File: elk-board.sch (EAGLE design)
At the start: 199 parts, among them IC1 ALLWINNER--H3, IC2 SY6280, IC3 K4B4G1646B-BCK0, IC4 RT8059GJ5, IC5 RT8059GJ5, IC6 SY8089A, IC7 NCP803SN263T1G, IC8 RT8059GJ5, IC9 MP2143DJ-LF-P, Q1 AO3415A, Q2 BCM856BS, Q3 9HT10-32.768KEZF-T, Q4 L2N7002WT1G, U1 AP6212, U2 STM32F411CEU6TR, X1 10118192-0001LF, X2 ST11-H, X3 IPEX-20279-001E, Y1 26MHz, Y2 24MHz

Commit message: Added emmc chip and integrated antenna
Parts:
- removed R53: 10K ohm, GHI-BasicComponents:RESISTOR-(INCH)-0402
- removed R54: 100K ohm, GHI-BasicComponents:RESISTOR-(INCH)-0402
- removed X2: ST11-H, JAE_By_element14_Batch_1:ST11-H
- removed X3: IPEX-20279-001E, Spark:IPEX-20279-001E
- added ANT1: AMCA31-2R450G-S1F-T3, AMCA31-2R450G-S1F-T3:AMCA31-2R450G-S1F-T3
- added C107, C108: 100nF, GHI-BasicComponents:CAPACITOR-(INCH)-0402
- added IC10: MP2143DJ-LF-P, MP2143DJ-LF-P:MP2143DJ-LF-P
- added L7: DFE252010P-2R2M=P2, DFE252010P-2R2M=P2:DFE252010P-2R2M=P2
- C1, C55, C7, C74, C79, C82: value 1uF -> 100nF
- C100, C25, C34, C44, C45, C56, C59, C66, C72, C73, C93, C96, C97: value 100nF -> 10uF; device GHI-BasicComponents:CAPACITOR-(INCH)-0402 -> GHI-BasicComponents:CAPACITOR-(INCH)-0603
- C101: value 22pF -> 10uF; device GHI-BasicComponents:CAPACITOR-(INCH)-0402 -> GHI-BasicComponents:CAPACITOR-(INCH)-0603
- C103: value 10uF -> 22pF; device GHI-BasicComponents:TOLBA_CAP -> GHI-BasicComponents:CAPACITOR-(INCH)-0402
- C104: value 10uF -> 100nF; device GHI-BasicComponents:TOLBA_CAP -> GHI-BasicComponents:CAPACITOR-(INCH)-0402
- C105, C106: value 100nF -> 10uF; device GHI-BasicComponents:CAPACITOR-(INCH)-0402 -> GHI-BasicComponents:TOLBA_CAP
- C12, C13, C47, C48: value 12pF -> 100nF
- C14: value 10uF -> 12pF; device GHI-BasicComponents:CAPACITOR-(INCH)-0603 -> GHI-BasicComponents:CAPACITOR-(INCH)-0402
- C15: value 10uF -> 12pF; device GHI-BasicComponents:TOLBA_CAP -> GHI-BasicComponents:CAPACITOR-(INCH)-0402
- C16: device GHI-BasicComponents:TOLBA_CAP -> GHI-BasicComponents:CAPACITOR-(INCH)-0603
- C17, C18: value 1uF -> 10uF; device GHI-BasicComponents:CAPACITOR-(INCH)-0402 -> GHI-BasicComponents:TOLBA_CAP
- C19: value 10pF -> 1uF
- C2, C23, C76, C8, C81, C84, C9: value 100nF -> 1uF
- C22: value 10uF -> 1.5pF; device GHI-BasicComponents:CAPACITOR-(INCH)-0603 -> GHI-BasicComponents:CAPACITOR-(INCH)-0402
- C24, C38, C4, C54, C61, C70, C92, C95, C98, C99: value 10uF -> 100nF; device GHI-BasicComponents:CAPACITOR-(INCH)-0603 -> GHI-BasicComponents:CAPACITOR-(INCH)-0402
- C27: value 100nF -> (none)
- C31: value 22uF -> 100nF; device GHI-BasicComponents:CAPACITOR-(INCH)-0603 -> GHI-BasicComponents:CAPACITOR-(INCH)-0402
- C32: value 10uF -> 22uF
- C37, C51, C58, C89: value 4.7uF -> 100nF
- C39, C91: value 10uF -> 4.7uF; device GHI-BasicComponents:CAPACITOR-(INCH)-0603 -> GHI-BasicComponents:CAPACITOR-(INCH)-0402
- C49, C50: value 100nF -> 12pF
- C5, C65: value 1uF -> 10uF; device GHI-BasicComponents:CAPACITOR-(INCH)-0402 -> GHI-BasicComponents:CAPACITOR-(INCH)-0603
- C53: value 100nF -> 4.7uF
- C57, C62, C69: value 10uF -> 1uF; device GHI-BasicComponents:CAPACITOR-(INCH)-0603 -> GHI-BasicComponents:CAPACITOR-(INCH)-0402
- C60: value 1uF -> 4.7uF
- C85, C86: value 18pF -> 100nF
- C87, C88: value 100nF -> 18pF
- IC1: value ALLWINNER--H3 -> KLM8G1GESD-B03P; device Allwinner_H3:ALLWINNER--H3 -> KLM8G1GESD-B03P:KLM8G1GESD-B03P
- IC2: value SY6280 -> ALLWINNER--H3; device SY6280:SY6280 -> Allwinner_H3:ALLWINNER--H3
- IC3: value K4B4G1646B-BCK0 -> SY6280; device K4B4G1646B-BCK0:K4B4G1646B-BCK0 -> SY6280:SY6280
- IC4: value RT8059GJ5 -> K4B4G1646B-BCK0; device RT8059GJ5:RT8059GJ5 -> K4B4G1646B-BCK0:K4B4G1646B-BCK0
- IC6: value SY8089A -> RT8059GJ5; device SY8089A:SY8089A -> RT8059GJ5:RT8059GJ5
- IC7: value NCP803SN263T1G -> SY8089A; device NCP803SN263T1G:NCP803SN263T1G -> SY8089A:SY8089A
- IC8: value RT8059GJ5 -> NCP803SN263T1G; device RT8059GJ5:RT8059GJ5 -> NCP803SN263T1G:NCP803SN263T1G
- IC9: value MP2143DJ-LF-P -> RT8059GJ5; device MP2143DJ-LF-P:MP2143DJ-LF-P -> RT8059GJ5:RT8059GJ5
- L2: value DFE252010P-2R2M=P2 -> 3.9nH; device DFE252010P-2R2M=P2:DFE252010P-2R2M=P2 -> Adafruit PowerBoost 1000C Rev B:MICROBUILDER_INDUCTOR_0402
- R10: value 22 ohm -> 100K ohm
- R14: value 33 ohm -> 6.8K ohm
- R15: value 6.8K ohm -> 10K ohm
- R16: value 10K ohm -> 2K ohm / 1%
- R18: value 2K ohm / 1% -> 100 ohm
- R19: value 100 ohm -> 10K ohm
- R24: value 10K ohm -> 10M ohm
- R25: value 10M ohm -> 6.8K ohm / 1%
- R26: value 6.8K ohm / 1% -> 47K ohm
- R27: value 47K ohm -> 240 ohm / 1%
- R29: value 240 ohm / 1% -> 10K ohm / 1%
- R3, R6: value 30K ohm -> 10K ohm
- R31, R36, R50: value 10K ohm / 1% -> 10K ohm
- R32: value 10K ohm -> 30K ohm / 1%
- R33: value 30K ohm / 1% -> 100K ohm
- R34: value 100K ohm -> 15K ohm / 1%
- R35: value 15K ohm / 1% -> 10K ohm / 1%
- R39: value 10K ohm -> 33 ohm
- R40: value 33 ohm -> 10K ohm
- R41: value 10K ohm -> 1K ohm
- R43: value 1K ohm -> 240 ohm / 1%
- R44: value 240 ohm / 1% -> 6.8K ohm / 1%
- R45: value 6.8K ohm / 1% -> 30K ohm / 1%
- R46: value 0 ohm -> 12K ohm / 1%
- R47: value 30K ohm / 1% -> 10K ohm / 1%
- R48: value 1K ohm -> 30K ohm / 1%
- R49: value 12K ohm / 1% -> 1K ohm
- R5: value 10K ohm -> 30K ohm
- R51: value 30K ohm / 1% -> 0 ohm
- R7: value 47K ohm -> 30K ohm
- R8: value 47K ohm -> 100K ohm
- R9: value 100K ohm -> 22 ohm
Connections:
- removed net N$15: C19.P$1, U1.WL_BT_ANT
- removed net N$16: C19.P$2, X3.1
- removed net N$30: R14.1, X2.CLK
- removed net SDC0_CLK: IC1G$1.PF2/SDC0_CLK/UART0_TX, R14.2
- removed net SDC0_CMD: IC1G$1.PF3/SDC0_CMD/JTAG_DO0, R8.1, X2.CMD
- removed net SDC0_D0: IC1G$1.PF1/SDC0_D0/JTAG_DI0, X2.DATA0
- removed net SDC0_D1: IC1G$1.PF0/SDC0_D1/JTAG_MS0, X2.DATA1
- removed net SDC0_D2: IC1G$1.PF5/SDC0_D2/JTAG_CK0, X2.DATA2
- removed net SDC0_D3: IC1G$1.PF4/SDC0_D3/UART0_RX, X2.CD/DATA3
- removed net SDC0_DET: IC1G$1.PF6, R7.1, X2.DSW2
- new net EMMC_CLK: IC1.CLK, IC2G$4.PC5/NAND_RE/SDC2_CLK
- new net EMMC_CMD: IC1.CMD, IC2G$4.PC6/NAND_RB0/SDC2_CMD, R3.1
- new net EMMC_D0: IC1.DAT0, IC2G$4.PC8/NAND_DQ0/SDC2_D0
- new net EMMC_D1: IC1.DAT1, IC2G$4.PC9/NAND_DQ1/SDC2_D1
- new net EMMC_D2: IC1.DAT2, IC2G$4.PC10/NAND_DQ2/SDC2_D2
- new net EMMC_D3: IC1.DAT3, IC2G$4.PC11/NAND_DQ3/SDC2_D3
- new net EMMC_D4: IC1.DAT4, IC2G$4.PC12/NAND_DQ4/SDC2_D4
- new net EMMC_D5: IC1.DAT5, IC2G$4.PC13/NAND_DQ5/SDC2_D5
- new net EMMC_D6: IC1.DAT6, IC2G$4.PC14/NAND_DQ6/SDC2_D6
- new net EMMC_D7: IC1.DAT7, IC2G$4.PC15/NAND_DQ7/SDC2_D7
- new net EMMC_RST: IC1.RSTN, IC2G$4.PC16/NAND_DQS/SDC2_RST
- new net N$12: ANT1.FEED, C27.P$2, L2.2
- new net N$20: C22.P$2, L2.1, U1.WL_BT_ANT
- new net VDDI_EMMC: C3.P$2, C7.P$2, IC1.VDDI
- net 1.2V: now also C19.P$1, C20.P$1, C23.P$1, C26.P$1, C29.P$1, C66.P$1, C72.P$1, C78.P$1, IC2G$2.EPHY_VDD, IC2G$6.VDD_SYS0, IC2G$6.VDD_SYS1, IC2G$6.VDD_SYS10, IC2G$6.VDD_SYS11, IC2G$6.VDD_SYS2, IC2G$6.VDD_SYS3, IC2G$6.VDD_SYS4, IC2G$6.VDD_SYS5, IC2G$6.VDD_SYS6, IC2G$6.VDD_SYS7, IC2G$6.VDD_SYS8, IC2G$6.VDD_SYS9, L5.2, R35.2; no longer C17.P$1, C18.P$1, C21.P$1, C25.P$1, C28.P$1, C64.P$1, C70.P$1, C76.P$1, IC1G$2.EPHY_VDD, IC1G$6.VDD_SYS0, IC1G$6.VDD_SYS1, IC1G$6.VDD_SYS10, IC1G$6.VDD_SYS11, IC1G$6.VDD_SYS2, IC1G$6.VDD_SYS3, IC1G$6.VDD_SYS4, IC1G$6.VDD_SYS5, IC1G$6.VDD_SYS6, IC1G$6.VDD_SYS7, IC1G$6.VDD_SYS8, IC1G$6.VDD_SYS9, L3.2, R36.2
- net 1.5V: now also C11.P$1, C12.P$1, C37.P$1, C52.P$1, C56.P$1, C57.P$1, C6.P$1, C62.P$1, C65.P$1, C68.P$1, C76.P$1, C77.P$1, C80.P$1, C84.P$1, C85.P$1, C92.P$1, IC2G$3.VCC_DRAM0, IC2G$3.VCC_DRAM1, IC2G$3.VCC_DRAM10, IC2G$3.VCC_DRAM2, IC2G$3.VCC_DRAM3, IC2G$3.VCC_DRAM4, IC2G$3.VCC_DRAM5, IC2G$3.VCC_DRAM6, IC2G$3.VCC_DRAM7, IC2G$3.VCC_DRAM8, IC2G$3.VCC_DRAM9, IC4.VDDQ_1, IC4.VDDQ_2, IC4.VDDQ_3, IC4.VDDQ_4, IC4.VDDQ_5, IC4.VDDQ_6, IC4.VDDQ_7, IC4.VDDQ_8, IC4.VDDQ_9, IC4.VDD_1, IC4.VDD_2, IC4.VDD_3, IC4.VDD_4, IC4.VDD_5, IC4.VDD_6, IC4.VDD_7, IC4.VDD_8, IC4.VDD_9, R16.2, R34.2; no longer C10.P$1, C35.P$1, C5.P$1, C50.P$1, C53.P$1, C54.P$1, C59.P$1, C60.P$1, C66.P$1, C67.P$1, C7.P$1, C74.P$1, C78.P$1, C79.P$1, C82.P$1, C88.P$1, IC1G$3.VCC_DRAM0, IC1G$3.VCC_DRAM1, IC1G$3.VCC_DRAM10, IC1G$3.VCC_DRAM2, IC1G$3.VCC_DRAM3, IC1G$3.VCC_DRAM4, IC1G$3.VCC_DRAM5, IC1G$3.VCC_DRAM6, IC1G$3.VCC_DRAM7, IC1G$3.VCC_DRAM8, IC1G$3.VCC_DRAM9, IC3.VDDQ_1, IC3.VDDQ_2, IC3.VDDQ_3, IC3.VDDQ_4, IC3.VDDQ_5, IC3.VDDQ_6, IC3.VDDQ_7, IC3.VDDQ_8, IC3.VDDQ_9, IC3.VDD_1, IC3.VDD_2, IC3.VDD_3, IC3.VDD_4, IC3.VDD_5, IC3.VDD_6, IC3.VDD_7, IC3.VDD_8, IC3.VDD_9, R17.2, R35.2
- net 3.3V: now also C1.P$2, C10.P$1, C101.P$1, C102.P$1, C108.P$1, C13.P$1, C30.P$1, C34.P$1, C35.P$1, C5.P$1, C54.P$1, C74.P$1, IC1.VDDF_1, IC1.VDDF_2, IC1.VDDF_3, IC1.VDDF_4, IC1.VDD_1, IC1.VDD_2, IC1.VDD_3, IC1.VDD_4, IC1.VDD_5, IC2G$1.VCC_PD, IC2G$2.AVCC, IC2G$2.EPHY_VCC, IC2G$2.HVCC, IC2G$2.V33_TV, IC2G$5.VCC_PG, IC2G$6.VCC_IO0, IC2G$6.VCC_IO1, IC2G$6.VCC_IO2, IC2G$6.VCC_IO3, IC2G$6.VCC_IO4, IC2G$6.VCC_IO5, IC2G$7.VCC_PLL, IC2G$7.VCC_RTC, IC2G$7.VCC_USB, IC2G$7.VDD_EFUSE, IC8.VCC, L6.2, R21.2, R26.1, R3.2, R31.1, R33.1, R36.1, R40.1, R45.2, R5.1, R50.2, R52.1, R6.2, R7.1, R8.1; no longer C106.P$1, C11.P$1, C2.P$2, C22.P$1, C26.P$1, C29.P$1, C32.P$1, C4.P$1, C52.P$1, C6.P$1, C72.P$1, C98.P$1, C99.P$1, IC1G$1.VCC_PD, IC1G$2.AVCC, IC1G$2.EPHY_VCC, IC1G$2.HVCC, IC1G$2.V33_TV, IC1G$5.VCC_PG, IC1G$6.VCC_IO0, IC1G$6.VCC_IO1, IC1G$6.VCC_IO2, IC1G$6.VCC_IO3, IC1G$6.VCC_IO4, IC1G$6.VCC_IO5, IC1G$7.VCC_PLL, IC1G$7.VCC_RTC, IC1G$7.VCC_USB, IC1G$7.VDD_EFUSE, IC7.VCC, L5.2, R24.2, R27.1, R3.1, R32.1, R34.1, R39.1, R41.1, R47.2, R5.2, R52.2, R53.1, R6.1, R7.2, R8.2, R9.1, X2.VDD
- net AP_RESET#: now also C89.P$1, IC2G$7.RESET, IC8.!RESET, R38.2; no longer C87.P$1, IC1G$7.RESET, IC7.!RESET, R39.2
- net BOOT0: now also IC2G$5.PG8/UART1_RTS/PG_EINT8, R20.1; no longer IC1G$5.PG8/UART1_RTS/PG_EINT8, R21.1
- net CPUX_VSET: now also IC2G$4.PC7/NAND_RB1, R50.1; no longer IC1G$4.PC5/NAND_RE/SDC2_CLK, R52.1
- net GND: now also C1.P$1, C101.P$2, C107.P$2, C108.P$2, C12.P$2, C13.P$2, C14.P$1, C15.P$1, C19.P$2, C2.P$2, C22.P$1, C27.P$1, C3.P$1, C34.P$2, C35.P$2, C36.P$1, C7.P$1, C85.P$2, C86.P$2, C87.P$1, C88.P$1, IC1.VSS_1, IC1.VSS_10, IC1.VSS_11, IC1.VSS_2, IC1.VSS_3, IC1.VSS_4, IC1.VSS_5, IC1.VSS_6, IC1.VSS_7, IC1.VSS_8, IC1.VSS_9, IC10.AGND, IC10.PGND, IC2G$2.AGND, IC2G$2.GND_TV, IC2G$2.HGND, IC2G$6.GND_CPUXFB, IC2G$8.GND0, IC2G$8.GND1, IC2G$8.GND10, IC2G$8.GND11, IC2G$8.GND12, IC2G$8.GND13, IC2G$8.GND14, IC2G$8.GND15, IC2G$8.GND16, IC2G$8.GND17, IC2G$8.GND18, IC2G$8.GND19, IC2G$8.GND2, IC2G$8.GND20, IC2G$8.GND21, IC2G$8.GND22, IC2G$8.GND23, IC2G$8.GND24, IC2G$8.GND25, IC2G$8.GND26, IC2G$8.GND27, IC2G$8.GND28, IC2G$8.GND29, IC2G$8.GND3, IC2G$8.GND30, IC2G$8.GND31, IC2G$8.GND32, IC2G$8.GND33, IC2G$8.GND34, IC2G$8.GND35, IC2G$8.GND36, IC2G$8.GND37, IC2G$8.GND38, IC2G$8.GND39, IC2G$8.GND4, IC2G$8.GND40, IC2G$8.GND41, IC2G$8.GND42, IC2G$8.GND43, IC2G$8.GND44, IC2G$8.GND45, IC2G$8.GND46, IC2G$8.GND47, IC2G$8.GND5, IC2G$8.GND6, IC2G$8.GND7, IC2G$8.GND8, IC2G$8.GND9, IC3.GND, IC4.VSSQ_1, IC4.VSSQ_2, IC4.VSSQ_3, IC4.VSSQ_4, IC4.VSSQ_5, IC4.VSSQ_6, IC4.VSSQ_7, IC4.VSSQ_8, IC4.VSSQ_9, IC4.VSS_1, IC4.VSS_10, IC4.VSS_11, IC4.VSS_12, IC4.VSS_2, IC4.VSS_3, IC4.VSS_4, IC4.VSS_5, IC4.VSS_6, IC4.VSS_7, IC4.VSS_8, IC4.VSS_9, IC9.GND, R10.1, R14.1, R17.1, R20.2, R25.1, R27.2, R29.1, R41.2, R43.1, R46.1; no longer C1.P$2, C103.P$2, C12.P$1, C13.P$1, C14.P$2, C15.P$2, C2.P$1, C22.P$2, C27.P$2, C3.P$2, C34.P$1, C36.P$2, C37.P$2, C7.P$2, C85.P$1, C86.P$1, C87.P$2, C88.P$2, IC1G$2.AGND, IC1G$2.GND_TV, IC1G$2.HGND, IC1G$6.GND_CPUXFB, IC1G$8.GND0, IC1G$8.GND1, IC1G$8.GND10, IC1G$8.GND11, IC1G$8.GND12, IC1G$8.GND13, IC1G$8.GND14, IC1G$8.GND15, IC1G$8.GND16, IC1G$8.GND17, IC1G$8.GND18, IC1G$8.GND19, IC1G$8.GND2, IC1G$8.GND20, IC1G$8.GND21, IC1G$8.GND22, IC1G$8.GND23, IC1G$8.GND24, IC1G$8.GND25, IC1G$8.GND26, IC1G$8.GND27, IC1G$8.GND28, IC1G$8.GND29, IC1G$8.GND3, IC1G$8.GND30, IC1G$8.GND31, IC1G$8.GND32, IC1G$8.GND33, IC1G$8.GND34, IC1G$8.GND35, IC1G$8.GND36, IC1G$8.GND37, IC1G$8.GND38, IC1G$8.GND39, IC1G$8.GND4, IC1G$8.GND40, IC1G$8.GND41, IC1G$8.GND42, IC1G$8.GND43, IC1G$8.GND44, IC1G$8.GND45, IC1G$8.GND46, IC1G$8.GND47, IC1G$8.GND5, IC1G$8.GND6, IC1G$8.GND7, IC1G$8.GND8, IC1G$8.GND9, IC2.GND, IC3.VSSQ_1, IC3.VSSQ_2, IC3.VSSQ_3, IC3.VSSQ_4, IC3.VSSQ_5, IC3.VSSQ_6, IC3.VSSQ_7, IC3.VSSQ_8, IC3.VSSQ_9, IC3.VSS_1, IC3.VSS_10, IC3.VSS_11, IC3.VSS_12, IC3.VSS_2, IC3.VSS_3, IC3.VSS_4, IC3.VSS_5, IC3.VSS_6, IC3.VSS_7, IC3.VSS_8, IC3.VSS_9, IC4.GND, IC9.AGND, IC9.PGND, R16.1, R18.1, R21.2, R26.1, R29.2, R31.1, R43.2, R45.1, R49.1, R54.1, X2.GND, X2.VSS, X3.GND@1
- net GPIOA15/SPI1_MOSI: now also IC2G$1.PA15/SPI1_MOSI/UART3_RTS/PA_EINT15, R39.1; no longer IC1G$1.PA15/SPI1_MOSI/UART3_RTS/PA_EINT15, R40.1
- net H3_UART1_RX: now also IC2G$5.PG7/UART1_RX/PG_EINT7; no longer IC1G$5.PG7/UART1_RX/PG_EINT7
- net H3_UART1_TX: now also IC2G$5.PG6/UART1_TX/PG_EINT6; no longer IC1G$5.PG6/UART1_TX/PG_EINT6
- net KERNEL_LED: now also IC2G$1.PD6/RGMII_NULL/MII_RXERR/RMII_RXER; no longer IC1G$1.PD6/RGMII_NULL/MII_RXERR/RMII_RXER
- net MCU_3.3V: now also C58.P$1, C59.P$1, C64.P$1, C67.P$1, C70.P$1, C79.P$1, C82.P$1, C86.P$1, C91.P$1, L3.2, R19.1, R32.2; no longer C56.P$1, C57.P$1, C62.P$1, C65.P$1, C68.P$1, C77.P$1, C80.P$1, C84.P$1, C89.P$1, L2.2, R20.1, R33.2
- net MCU_REG_EN: now also IC2G$1.PD1/RGMII_RXD2/MII_RXD2/RMII_NULL/DI_RX, IC5.EN, R21.1; no longer IC1G$1.PD1/RGMII_RXD2/MII_RXD2/RMII_NULL/DI_RX, IC4.EN, R22.1
- net MCU_RST: now also C36.P$2, IC2G$5.PG13/PCM1_DIN/PG_EINT13, R19.2; no longer C34.P$2, IC1G$5.PG13/PCM1_DIN/PG_EINT13, R20.2
- net N$1: now also R9.1; no longer R10.1
- net N$10: now also C14.P$2; no longer C12.P$2
- net N$11: now also R49.2; no longer R48.2
- net N$13: now also R39.2; no longer R40.2
- net N$14: now also C25.P$1; no longer C24.P$1
- net N$18: now also IC6.FB, R29.2, R34.1; no longer IC5.FB, R30.2, R35.1
- net N$19: now also IC7.LX, L5.1; no longer IC6.LX, L3.1
- net N$2: now also R51.2; no longer R46.2
- net N$21: now also R41.1; no longer R42.1
- net N$22: now also C39.P$1; no longer C37.P$1
- net N$26: now also IC4.ZQ, R27.1; no longer IC3.ZQ, R28.1
- net N$28: now also C16.P$1, IC3.OUT; no longer C14.P$1, IC2.OUT
- net N$3: now also IC5.LX, L3.1; no longer IC4.LX, L2.1
- net N$33: now also IC7.FB, R30.2, R35.1; no longer IC6.FB, R31.2, R36.1
- net N$35: now also C49.P$1, IC2G$7.X32KIN, R24.2; no longer C47.P$1, IC1G$7.X32KIN, R25.2
- net N$36: now also IC10.SW, L7.1; no longer IC9.SW, L6.1
- net N$37: now also C103.P$2, IC10.FB, R46.2, R47.1, R48.2; no longer C101.P$2, IC9.FB, R49.2, R50.1, R51.2
- net N$38: now also IC3.ISET, R14.2; no longer IC2.ISET, R15.2
- net N$40: now also IC9.LX, L6.1; no longer IC8.LX, L5.1
- net N$41: now also IC2G$3.SZQ, R43.2; no longer IC1G$3.SZQ, R44.2
- net N$42: now also IC9.FB, R44.2, R45.1; no longer IC8.FB, R45.2, R47.1
- net N$44: now also R48.1; no longer R51.1
- net N$48: now also C50.P$1, IC2G$7.X32KOUT, R24.1; no longer C48.P$1, IC1G$7.X32KOUT, R25.1
- net N$5: now also R42.1; no longer R43.1
- net N$50: now also C60.P$1, IC2G$7.VDD_EFUSEBP; no longer C58.P$1, IC1G$7.VDD_EFUSEBP
- net N$51: now also IC2G$7.NMI, R26.2; no longer IC1G$7.NMI, R27.2
- net N$52: now also IC2G$7.KEYADC, R33.2; no longer IC1G$7.KEYADC, R34.2
- net N$6: now also IC6.LX; no longer IC5.LX
- net N$7: now also R10.2; no longer R54.2
- net N$74: now also IC4.NC_4, R28.1; no longer IC3.NC_4, R29.1
- net N$8: now also IC5.FB, R25.2, R32.1; no longer IC4.FB, R26.2, R33.1
- net N$9: now also C15.P$2; no longer C13.P$2
- net PWR_DRAM: now also IC2G$1.PA21/PCM0_DIN/SIM_VPPPP/PA_EINT21, IC6.EN, R22.1; no longer IC1G$1.PA21/PCM0_DIN/SIM_VPPPP/PA_EINT21, IC5.EN, R23.1
- net PWR_STB: now also IC10.EN, IC2G$1.PD4/RGMII_RXCK/MII_RXCK/RMII_NULL, IC7.EN, R23.1; no longer IC1G$1.PD4/RGMII_RXCK/MII_RXCK/RMII_NULL, IC6.EN, IC9.EN, R24.1
- net RESET_SW: now also IC2G$1.PA8/SIM_DATA/PA_EINT8, R52.2; no longer IC1G$1.PA8/SIM_DATA/PA_EINT8, R53.2
- net SA0: now also IC2G$3.SA0, IC4.A0; no longer IC1G$3.SA0, IC3.A0
- net SA1: now also IC2G$3.SA1, IC4.A1; no longer IC1G$3.SA1, IC3.A1
- net SA10: now also IC2G$3.SA10, IC4.A10/AP; no longer IC1G$3.SA10, IC3.A10/AP
- net SA11: now also IC2G$3.SA11, IC4.A11; no longer IC1G$3.SA11, IC3.A11
- net SA12: now also IC2G$3.SA12, IC4.A12/!BC; no longer IC1G$3.SA12, IC3.A12/!BC
- net SA13: now also IC2G$3.SA13, IC4.A13; no longer IC1G$3.SA13, IC3.A13
- net SA14: now also IC2G$3.SA14, IC4.A14; no longer IC1G$3.SA14, IC3.A14
- net SA15: now also IC2G$3.SA15, IC4.NC_5; no longer IC1G$3.SA15, IC3.NC_5
- net SA2: now also IC2G$3.SA2, IC4.A2; no longer IC1G$3.SA2, IC3.A2
- net SA3: now also IC2G$3.SA3, IC4.A3; no longer IC1G$3.SA3, IC3.A3
- net SA4: now also IC2G$3.SA4, IC4.A4; no longer IC1G$3.SA4, IC3.A4
- net SA5: now also IC2G$3.SA5, IC4.A5; no longer IC1G$3.SA5, IC3.A5
- net SA6: now also IC2G$3.SA6, IC4.A6; no longer IC1G$3.SA6, IC3.A6
- net SA7: now also IC2G$3.SA7, IC4.A7; no longer IC1G$3.SA7, IC3.A7
- net SA8: now also IC2G$3.SA8, IC4.A8; no longer IC1G$3.SA8, IC3.A8
- net SA9: now also IC2G$3.SA9, IC4.A9; no longer IC1G$3.SA9, IC3.A9
- net SBA0: now also IC2G$3.SBA0, IC4.BA0; no longer IC1G$3.SBA0, IC3.BA0
- net SBA1: now also IC2G$3.SBA1, IC4.BA1; no longer IC1G$3.SBA1, IC3.BA1
- net SBA2: now also IC2G$3.SBA2, IC4.BA2; no longer IC1G$3.SBA2, IC3.BA2
- net SCAS: now also IC2G$3.SCAS, IC4.!CAS; no longer IC1G$3.SCAS, IC3.!CAS
- net SCKE0: now also IC2G$3.SCKE0, IC4.CKE; no longer IC1G$3.SCKE0, IC3.CKE
- net SCKE1: now also IC2G$3.SCKE1, IC4.NC_2; no longer IC1G$3.SCKE1, IC3.NC_2
- net SCK_N: now also IC2G$3.SCKB, IC4.!CK, R18.1; no longer IC1G$3.SCKB, IC3.!CK, R19.1
- net SCK_P: now also IC2G$3.SCK, IC4.CK, R18.2; no longer IC1G$3.SCK, IC3.CK, R19.2
- net SCS0: now also IC2G$3.SCS0, IC4.!CS; no longer IC1G$3.SCS0, IC3.!CS
- net SCS1: now also IC2G$3.SCS1, IC4.NC_3; no longer IC1G$3.SCS1, IC3.NC_3
- net SDC1_CLK: now also IC2G$5.PG0/SDC1_CLK/PG_EINT0, R9.2; no longer IC1G$5.PG0/SDC1_CLK/PG_EINT0, R10.2
- net SDC1_CMD: now also IC2G$5.PG1/SDC1_CMD/PG_EINT1, R7.2; no longer IC1G$5.PG1/SDC1_CMD/PG_EINT1, R6.2
- net SDC1_D0: now also IC2G$5.PG2/SDC1_D0/PG_EINT2, R5.2; no longer IC1G$5.PG2/SDC1_D0/PG_EINT2, R4.2
- net SDC1_D1: now also IC2G$5.PG3/SDC1_D1/PG_EINT3, R4.2; no longer IC1G$5.PG3/SDC1_D1/PG_EINT3, R3.2
- net SDC1_D2: now also IC2G$5.PG4/SDC1_D2/PG_EINT4; no longer IC1G$5.PG4/SDC1_D2/PG_EINT4
- net SDC1_D3: now also IC2G$5.PG5/SDC1_D3/PG_EINT5; no longer IC1G$5.PG5/SDC1_D3/PG_EINT5
- net SDQ0: now also IC2G$3.SDQ0, IC4.DQL1; no longer IC1G$3.SDQ0, IC3.DQL1
- net SDQ1: now also IC2G$3.SDQ1, IC4.DQL5; no longer IC1G$3.SDQ1, IC3.DQL5
- net SDQ10: now also IC2G$3.SDQ10, IC4.DQU7; no longer IC1G$3.SDQ10, IC3.DQU7
- net SDQ11: now also IC2G$3.SDQ11, IC4.DQU6; no longer IC1G$3.SDQ11, IC3.DQU6
- net SDQ12: now also IC2G$3.SDQ12, IC4.DQU2; no longer IC1G$3.SDQ12, IC3.DQU2
- net SDQ13: now also IC2G$3.SDQ13, IC4.DQU0; no longer IC1G$3.SDQ13, IC3.DQU0
- net SDQ14: now also IC2G$3.SDQ14, IC4.DQU1; no longer IC1G$3.SDQ14, IC3.DQU1
- net SDQ15: now also IC2G$3.SDQ15, IC4.DQU3; no longer IC1G$3.SDQ15, IC3.DQU3
- net SDQ2: now also IC2G$3.SDQ2, IC4.DQL3; no longer IC1G$3.SDQ2, IC3.DQL3
- net SDQ3: now also IC2G$3.SDQ3, IC4.DQL4; no longer IC1G$3.SDQ3, IC3.DQL4
- net SDQ4: now also IC2G$3.SDQ4, IC4.DQL7; no longer IC1G$3.SDQ4, IC3.DQL7
- net SDQ5: now also IC2G$3.SDQ5, IC4.DQL0; no longer IC1G$3.SDQ5, IC3.DQL0
- net SDQ6: now also IC2G$3.SDQ6, IC4.DQL6; no longer IC1G$3.SDQ6, IC3.DQL6
- net SDQ7: now also IC2G$3.SDQ7, IC4.DQL2; no longer IC1G$3.SDQ7, IC3.DQL2
- net SDQ8: now also IC2G$3.SDQ8, IC4.DQU4; no longer IC1G$3.SDQ8, IC3.DQU4
- net SDQ9: now also IC2G$3.SDQ9, IC4.DQU5; no longer IC1G$3.SDQ9, IC3.DQU5
- net SDQM0: now also IC2G$3.SDQM0, IC4.DML; no longer IC1G$3.SDQM0, IC3.DML
- net SDQM1: now also IC2G$3.SDQM1, IC4.DMU; no longer IC1G$3.SDQM1, IC3.DMU
- net SDQS0_N: now also IC2G$3.SDQSB0, IC4.!DQSL; no longer IC1G$3.SDQSB0, IC3.!DQSL
- net SDQS0_P: now also IC2G$3.SDQS0, IC4.DQSL; no longer IC1G$3.SDQS0, IC3.DQSL
- net SDQS1_N: now also IC2G$3.SDQSB1, IC4.!DQSU; no longer IC1G$3.SDQSB1, IC3.!DQSU
- net SDQS1_P: now also IC2G$3.SDQS1, IC4.DQSU; no longer IC1G$3.SDQS1, IC3.DQSU
- net SETUP_SW: now also IC2G$1.PA20/PCM0_DOUT/SIM_VPPEN/PA_EINT20, R40.2; no longer IC1G$1.PA20/PCM0_DOUT/SIM_VPPEN/PA_EINT20, R41.2
- net SODT0: now also IC2G$3.SODT0, IC4.ODT; no longer IC1G$3.SODT0, IC3.ODT
- net SODT1: now also IC2G$3.SODT1, IC4.NC_1; no longer IC1G$3.SODT1, IC3.NC_1
- net SRAS: now also IC2G$3.SRAS, IC4.!RAS; no longer IC1G$3.SRAS, IC3.!RAS
- net SRST: now also IC2G$3.SRST, IC4.!RESET; no longer IC1G$3.SRST, IC3.!RESET
- net SVREF: now also C104.P$1, C37.P$2, C38.P$1, C51.P$1, IC2G$3.SVREF, IC4.VREFCA, IC4.VREFDQ, R16.1, R17.2; no longer C102.P$1, C35.P$2, C36.P$1, C49.P$1, IC1G$3.SVREF, IC3.VREFCA, IC3.VREFDQ, R17.1, R18.2
- net SWE: now also IC2G$3.SWE, IC4.!WE; no longer IC1G$3.SWE, IC3.!WE
- net UART0_RX: now also IC2G$1.PA5/UART0_RX/PWM0/PA_EINT5, R51.1; no longer IC1G$1.PA5/UART0_RX/PWM0/PA_EINT5, R46.1
- net UART0_TX: now also IC2G$1.PA4/UART0_TX/PA_EINT4, R49.1; no longer IC1G$1.PA4/UART0_TX/PA_EINT4, R48.1
- net UBOOT: now also IC2G$7.UBOOT, R36.2; no longer IC1G$7.UBOOT, R38.2
- net USB0_DRVVBUS: now also IC2G$4.PC2/NAND_CLE/SPI0_CLK, IC3.EN, R15.2; no longer IC1G$4.PC11/NAND_DQ3/SDC2_D3, IC2.EN, R16.2
- net USB0_N: now also IC2G$7.USB_DM0; no longer IC1G$7.USB_DM0
- net USB0_OTGID: now also IC2G$5.PG12/PCM1_DOUT/PG_EINT12, R6.1; no longer IC1G$5.PG12/PCM1_DOUT/PG_EINT12, R5.1
- net USB0_P: now also IC2G$7.USB_DP0; no longer IC1G$7.USB_DP0
- net VDD_CPUFB: now also C103.P$1, IC2G$6.VDD_CPUXFB, R47.2; no longer C101.P$1, IC1G$6.VDD_CPUXFB, R50.2
- net VDD_CPUS: now also C2.P$1, C4.P$1, C53.P$1, IC2G$6.VDD_CPUS0, IC2G$6.VDD_CPUS1, IC2G$7.RTC_VIO; no longer C1.P$1, C3.P$1, C51.P$1, IC1G$6.VDD_CPUS0, IC1G$6.VDD_CPUS1, IC1G$7.RTC_VIO
- net VDD_CPUX: now also C106.P$1, C107.P$1, C17.P$1, C18.P$1, C21.P$1, C24.P$1, C28.P$1, C31.P$1, IC10.OUT, IC2G$6.VDD_CPUX0, IC2G$6.VDD_CPUX1, IC2G$6.VDD_CPUX10, IC2G$6.VDD_CPUX11, IC2G$6.VDD_CPUX12, IC2G$6.VDD_CPUX2, IC2G$6.VDD_CPUX3, IC2G$6.VDD_CPUX4, IC2G$6.VDD_CPUX5, IC2G$6.VDD_CPUX6, IC2G$6.VDD_CPUX7, IC2G$6.VDD_CPUX8, IC2G$6.VDD_CPUX9, L7.2; no longer C103.P$1, C104.P$1, C15.P$1, C16.P$1, C20.P$1, C23.P$1, C27.P$1, C30.P$1, IC1G$6.VDD_CPUX0, IC1G$6.VDD_CPUX1, IC1G$6.VDD_CPUX10, IC1G$6.VDD_CPUX11, IC1G$6.VDD_CPUX12, IC1G$6.VDD_CPUX2, IC1G$6.VDD_CPUX3, IC1G$6.VDD_CPUX4, IC1G$6.VDD_CPUX5, IC1G$6.VDD_CPUX6, IC1G$6.VDD_CPUX7, IC1G$6.VDD_CPUX8, IC1G$6.VDD_CPUX9, IC9.OUT, L6.2
- net VIN: now also C32.P$1, C47.P$1, C48.P$1, C98.P$1, C99.P$1, IC10.VIN, IC3.IN, IC6.VIN, IC7.IN, IC9.EN; no longer C31.P$1, C38.P$1, C39.P$1, C91.P$1, C92.P$1, IC2.IN, IC4.VIN, IC6.IN, IC8.EN, IC8.VIN
- net WIFI_32K: now also IC2G$7.X32KFOUT, R31.2; no longer IC1G$7.X32KFOUT, R32.2
- net WL_REG_ON: now also IC2G$9.PL7/S_JTAG_SI/S_PL_EINT7; no longer IC1G$9.PL7/S_JTAG_SI/S_PL_EINT7
- net WL_WAKE_HOST: now also IC2G$5.PG10/PCM1_SYNC/PG_EINT10, R8.2; no longer IC1G$5.PG10/PCM1_SYNC/PG_EINT10, R9.2
- net X24_IN: now also C87.P$2, IC2G$7.X24MIN; no longer C85.P$2, IC1G$7.X24MIN
- net X24_OUT: now also C88.P$2, IC2G$7.X24MOUT; no longer C86.P$2, IC1G$7.X24MOUT
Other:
- note removed: "Only DATA[0:3] need length matching"
- note removed: "uSD Connector"
- moved on the sheet: C1, C10, C100, C101, C102, C103, C104, C105, C106, C11, C12, C13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

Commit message: Finished emmc and antenna (WIP)
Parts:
- L2: device Adafruit PowerBoost 1000C Rev B:MICROBUILDER_INDUCTOR_0402 -> Nordic_nRF:INDUCTOR_0402_L
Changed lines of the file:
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@@
 </layers>
 <schematic xreflabel="%F%N/%S.%C%R" xrefpart="/%S.%C%R">
-<fusionteam huburn="a.YnVzaW5lc3M6ZWxrcmVt" projecturn="a.YnVzaW5lc3M6ZWxrcmVtIzIwMTkwNTE0MTkzNzY0NjI2" folderUrn="urn:adsk.wipprod:fs.folder:co.lM7F2dEtQpysUSzvypi4-Q" urn="urn:adsk.wipprod:dm.lineage:Se4qbmlATyubusVm2n9KuA"  versionUrn="urn:adsk.wipprod:fs.file:vf.Se4qbmlATyubusVm2n9KuA?version=24" camFileUrn="" camFileVersionUrn="" lastpublishedchangeguid="8b6fd80a-dbfd-1cff-e868-49cbea7d7d36"/>
+<fusionteam huburn="a.YnVzaW5lc3M6ZWxrcmVt" projecturn="a.YnVzaW5lc3M6ZWxrcmVtIzIwMTkwNTE0MTkzNzY0NjI2" folderUrn="urn:adsk.wipprod:fs.folder:co.U9XNDY5QRfqUZXJ892w5Yg" urn="urn:adsk.wipprod:dm.lineage:FdQPUJtxQbmN-6sV6-on_w"  versionUrn="urn:adsk.wipprod:fs.file:vf.FdQPUJtxQbmN-6sV6-on_w?version=2" camFileUrn="" camFileVersionUrn="" lastpublishedchangeguid="486159d2-3dfa-844d-1c70-05aee61310eb"/>
 <attributes>
 </attributes>
@@
 <part name="GND4" library="supply1" library_urn="urn:adsk.eagle:library:371" deviceset="GND" device=""/>
 <part name="3.3V4" library="microbuilder" deviceset="3.3V" device=""/>
-<part name="L2" library="Adafruit PowerBoost 1000C Rev B" deviceset="MICROBUILDER_INDUCTOR" device="_0402" value="3.9nH"/>
+<part name="L2" library="Nordic_nRF" deviceset="INDUCTOR" device="_0402_L" package3d_urn="urn:adsk.eagle:package:2593728/1" value="3.9nH"/>
 <part name="GND21" library="supply1" library_urn="urn:adsk.eagle:library:371" deviceset="GND" device=""/>
 <part name="ANT1" library="AMCA31-2R450G-S1F-T3" deviceset="AMCA31-2R450G-S1F-T3" device=""/>
@@
 <attribute name="VALUE" x="51.816" y="282.956" size="1.27" layer="96"/>
 </instance>
-<instance part="L2" gate="G$1" x="190.5" y="142.24" smashed="yes">
-<attribute name="NAME" x="190.5" y="144.78" size="1.27" layer="95" align="center"/>
-<attribute name="VALUE" x="190.5" y="140.7" size="1.27" layer="96" align="center"/>
+<instance part="L2" gate="L$1" x="190.5" y="142.24" smashed="yes" rot="R90">
+<attribute name="NAME" x="185.42" y="144.78" size="1.27" layer="95" rot="R180" align="center"/>
+<attribute name="VALUE" x="195.58" y="144.78" size="1.27" layer="96" rot="R180" align="center"/>
 </instance>
 <instance part="GND21" gate="1" x="177.8" y="129.54" smashed="yes">
@@
 <segment>
 <pinref part="U1" gate="G$1" pin="WL_BT_ANT"/>
-<pinref part="L2" gate="G$1" pin="1"/>
-<wire x1="185.42" y1="142.24" x2="177.8" y2="142.24" width="0.1524" layer="91"/>
+<pinref part="L2" gate="L$1" pin="1"/>
+<wire x1="182.88" y1="142.24" x2="177.8" y2="142.24" width="0.1524" layer="91"/>
 <wire x1="177.8" y1="142.24" x2="168.402" y2="142.24" width="0.1524" layer="91"/>
 <wire x1="168.402" y1="142.24" x2="168.402" y2="137.16" width="0.1524" layer="91"/>
@@
 <net name="N$12" class="0">
 <segment>
-<pinref part="L2" gate="G$1" pin="2"/>
+<pinref part="L2" gate="L$1" pin="2"/>
 <pinref part="ANT1" gate="G$1" pin="FEED"/>
-<wire x1="195.58" y1="142.24" x2="200.66" y2="142.24" width="0.1524" layer="91"/>
+<wire x1="198.12" y1="142.24" x2="200.66" y2="142.24" width="0.1524" layer="91"/>
 <pinref part="C27" gate="G$1" pin="P$2"/>
 <wire x1="200.66" y1="142.24" x2="208.28" y2="142.24" width="0.1524" layer="91"/>

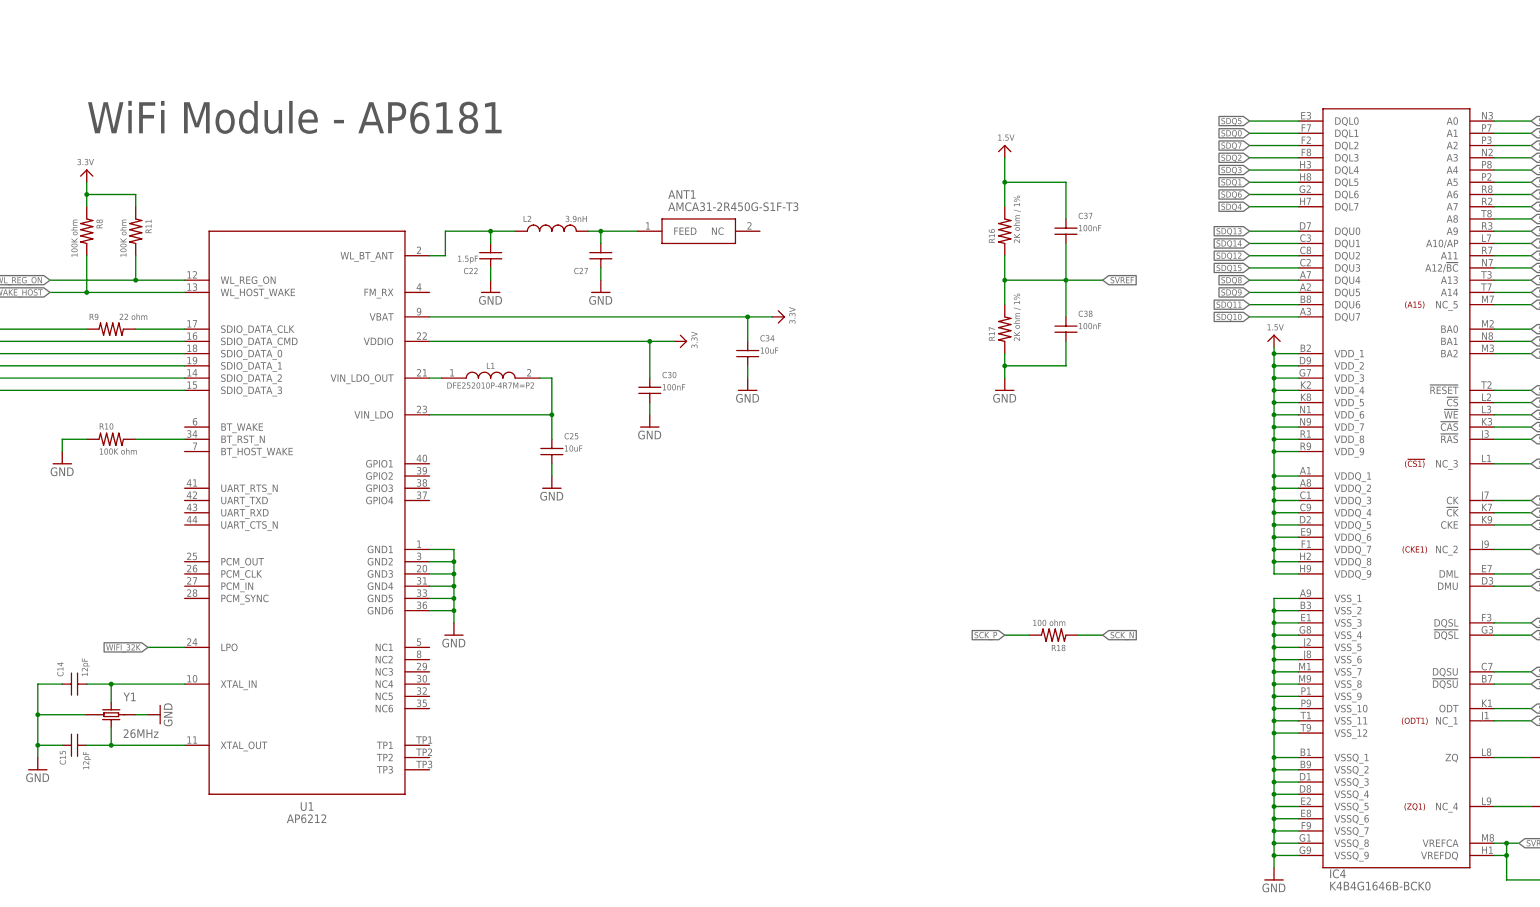
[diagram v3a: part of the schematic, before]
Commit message: Changed the RAM part Number in the schematic and modified the Wifi module label
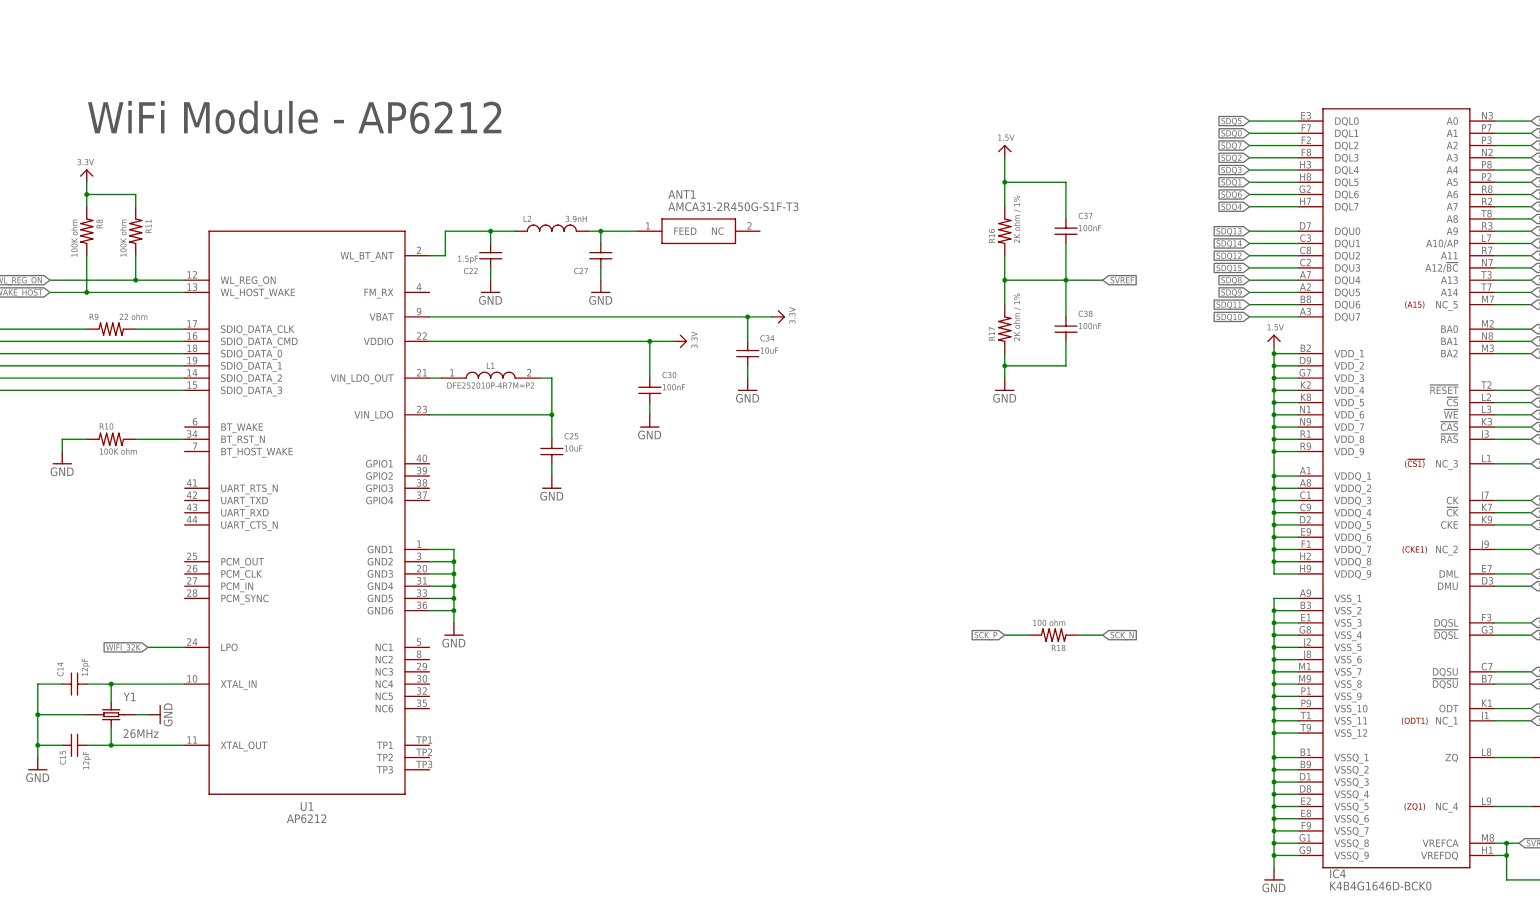
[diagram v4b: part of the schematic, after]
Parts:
- IC4: value K4B4G1646B-BCK0 -> K4B4G1646D-BCK0
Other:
- note added: "WiFi Module - AP6212"
- note removed: "WiFi Module - AP6181"
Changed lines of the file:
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@@
 <part name="R8" library="GHI-BasicComponents" deviceset="RESISTOR-(INCH)-" device="0402" value="100K ohm"/>
 <part name="FRAME11" library="frames" library_urn="urn:adsk.eagle:library:229" deviceset="A4L-LOC" device=""/>
-<part name="IC4" library="K4B4G1646B-BCK0" deviceset="K4B4G1646B-BCK0" device=""/>
+<part name="IC4" library="K4B4G1646B-BCK0" deviceset="K4B4G1646B-BCK0" device="" value="K4B4G1646D-BCK0"/>
 <part name="GND42" library="supply1" library_urn="urn:adsk.eagle:library:371" deviceset="GND" device=""/>
 <part name="R27" library="GHI-BasicComponents" deviceset="RESISTOR-(INCH)-" device="0402" value="240 ohm / 1%"/>
@@
 <sheet>
 <plain>
-<text x="93.98" y="162.56" size="6.4516" layer="97">WiFi Module - AP6181</text>
+<text x="93.98" y="162.56" size="6.4516" layer="97">WiFi Module - AP6212</text>
 <text x="444.5" y="162.56" size="6.4516" layer="97">DDR3 RAM</text>
 <text x="393.7" y="885.19" size="5.08" layer="97" align="bottom-center">MCU Voltage Regulator 3.3V /1A</text>

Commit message: Decrease LEDs brightness + MCU_REG_ON (Pull Down)
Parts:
- R37, R41, R42: value 1K ohm -> 1.5K ohm
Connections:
- net 3.3V: no longer R21.2
- net GND: now also R21.2
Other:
- moved on the sheet: R21
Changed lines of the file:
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@@
 <part name="FRAME10" library="frames" library_urn="urn:adsk.eagle:library:229" deviceset="A4L-LOC" device=""/>
 <part name="FRAME15" library="frames" library_urn="urn:adsk.eagle:library:229" deviceset="A4L-LOC" device=""/>
-<part name="R37" library="GHI-BasicComponents" deviceset="RESISTOR-(INCH)-" device="0402" value="1K ohm"/>
+<part name="R37" library="GHI-BasicComponents" deviceset="RESISTOR-(INCH)-" device="0402" value="1.5K ohm"/>
 <part name="GND70" library="supply1" deviceset="GND" device=""/>
 <part name="C58" library="GHI-BasicComponents" deviceset="CAPACITOR-(INCH)-" device="0402" value="100nF"/>
@@
 <part name="R21" library="GHI-BasicComponents" deviceset="RESISTOR-(INCH)-" device="0402" value="10K ohm"/>
 <part name="3.3V5" library="microbuilder" deviceset="3.3V" device=""/>
-<part name="3.3V12" library="microbuilder" deviceset="3.3V" device=""/>
 <part name="3.3V7" library="microbuilder" deviceset="3.3V" device=""/>
 <part name="3.3V14" library="microbuilder" deviceset="3.3V" device=""/>
@@
 <part name="3.3V6" library="microbuilder" deviceset="3.3V" device=""/>
 <part name="LED3" library="GHI-BasicComponents" deviceset="LED-(INCH)-" device="0603" value="BLUE"/>
-<part name="R42" library="GHI-BasicComponents" deviceset="RESISTOR-(INCH)-" device="0402" value="1K ohm"/>
+<part name="R42" library="GHI-BasicComponents" deviceset="RESISTOR-(INCH)-" device="0402" value="1.5K ohm"/>
 <part name="GND83" library="supply1" deviceset="GND" device=""/>
 <part name="C1" library="GHI-BasicComponents" deviceset="CAPACITOR-(INCH)-" device="0402" value="100nF"/>
@@
 <part name="S1" library="Spark" deviceset="TAC_SWITCH" device="SMD" value="KMR231GLFS"/>
 <part name="LED2" library="GHI-BasicComponents" deviceset="LED-(INCH)-" device="0603" value="RED"/>
-<part name="R41" library="GHI-BasicComponents" deviceset="RESISTOR-(INCH)-" device="0402" value="1K ohm"/>
+<part name="R41" library="GHI-BasicComponents" deviceset="RESISTOR-(INCH)-" device="0402" value="1.5K ohm"/>
 <part name="GND82" library="supply1" deviceset="GND" device=""/>
 <part name="3.3V24" library="microbuilder" deviceset="3.3V" device=""/>
@@
 <part name="C27" library="GHI-BasicComponents" deviceset="CAPACITOR-(INCH)-" device="0402"/>
 <part name="GND24" library="supply1" library_urn="urn:adsk.eagle:library:371" deviceset="GND" device=""/>
+<part name="GND98" library="supply1" deviceset="GND" device=""/>
 </parts>
 <sheets>
@@
 <attribute name="VALUE" x="320.04" y="814.705" size="1.778" layer="96"/>
 </instance>
-<instance part="GND43" gate="1" x="358.14" y="822.325" smashed="yes">
-<attribute name="VALUE" x="355.6" y="819.785" size="1.778" layer="96"/>
+<instance part="GND43" gate="1" x="358.14" y="824.865" smashed="yes">
+<attribute name="VALUE" x="355.6" y="822.325" size="1.778" layer="96"/>
 </instance>
 <instance part="VIN3" gate="G$1" x="322.58" y="843.28" smashed="yes">
 <attribute name="VALUE" x="321.056" y="844.296" size="1.27" layer="96"/>
 </instance>
-<instance part="R21" gate="G$1" x="353.06" y="845.82" smashed="yes" rot="R90">
-<attribute name="NAME" x="351.028" y="843.28" size="1.27" layer="95" font="vector" rot="R90"/>
-<attribute name="VALUE" x="356.235" y="843.28" size="1.27" layer="96" font="vector" rot="R90"/>
+<instance part="R21" gate="G$1" x="353.06" y="815.34" smashed="yes" rot="R270">
+<attribute name="NAME" x="355.092" y="817.88" size="1.27" layer="95" font="vector" rot="R270"/>
+<attribute name="VALUE" x="349.885" y="817.88" size="1.27" layer="96" font="vector" rot="R270"/>
 </instance>
 <instance part="3.3V5" gate="G$1" x="63.5" y="838.2" smashed="yes">
 <attribute name="VALUE" x="61.976" y="839.216" size="1.27" layer="96"/>
 </instance>
-<instance part="3.3V12" gate="G$1" x="353.06" y="858.52" smashed="yes">
-<attribute name="VALUE" x="351.536" y="859.536" size="1.27" layer="96"/>
-</instance>
 <instance part="3.3V7" gate="G$1" x="114.3" y="635" smashed="yes">
 <attribute name="VALUE" x="112.776" y="636.016" size="1.27" layer="96"/>
@@
 <attribute name="VALUE" x="198.12" y="127" size="1.778" layer="96"/>
 </instance>
+<instance part="GND98" gate="1" x="353.06" y="804.545" smashed="yes">
+<attribute name="VALUE" x="350.52" y="802.005" size="1.778" layer="96"/>
+</instance>
 </instances>
 <busses>
@@
 <pinref part="GND43" gate="1" pin="GND"/>
 <wire x1="360.68" y1="830.58" x2="358.14" y2="830.58" width="0.1524" layer="91"/>
-<wire x1="358.14" y1="830.58" x2="358.14" y2="824.865" width="0.1524" layer="91"/>
+<wire x1="358.14" y1="830.58" x2="358.14" y2="827.405" width="0.1524" layer="91"/>
 </segment>
 <segment>
@@
 <wire x1="200.66" y1="132.08" x2="200.66" y2="134.62" width="0.1524" layer="91"/>
 </segment>
+<segment>
+<pinref part="GND98" gate="1" pin="GND"/>
+<pinref part="R21" gate="G$1" pin="2"/>
+<wire x1="353.06" y1="807.085" x2="353.06" y2="810.26" width="0.1524" layer="91"/>
+</segment>
 </net>
 <net name="N$1" class="9">
@@
 </segment>
 <segment>
-<pinref part="R21" gate="G$1" pin="2"/>
-<wire x1="353.06" y1="850.9" x2="353.06" y2="855.98" width="0.1524" layer="91"/>
-<pinref part="3.3V12" gate="G$1" pin="3.3V"/>
-</segment>
-<segment>
 <pinref part="IC2" gate="G$6" pin="VCC_IO0"/>
 <wire x1="109.22" y1="629.92" x2="114.3" y2="629.92" width="0.1524" layer="91"/>
@@
 <pinref part="IC5" gate="G$1" pin="EN"/>
 <wire x1="360.68" y1="833.12" x2="353.06" y2="833.12" width="0.1524" layer="91"/>
-<wire x1="353.06" y1="833.12" x2="353.06" y2="840.74" width="0.1524" layer="91"/>
-<wire x1="353.06" y1="833.12" x2="353.06" y2="805.18" width="0.1524" layer="91"/>
+<wire x1="353.06" y1="833.12" x2="353.06" y2="820.42" width="0.1524" layer="91"/>
+<wire x1="353.06" y1="833.12" x2="353.06" y2="845.82" width="0.1524" layer="91"/>
 <junction x="353.06" y="833.12"/>
-<wire x1="353.06" y1="805.18" x2="335.28" y2="805.18" width="0.1524" layer="91"/>
-<label x="335.28" y="805.18" size="1.27" layer="95" font="vector" rot="R180" xref="yes"/>
+<wire x1="353.06" y1="845.82" x2="340.36" y2="845.82" width="0.1524" layer="91"/>
+<label x="340.36" y="845.82" size="1.27" layer="95" font="vector" rot="R180" xref="yes"/>
 </segment>
 <segment>
